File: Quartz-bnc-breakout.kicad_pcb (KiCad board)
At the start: 2 copper layers, 196.8 x 69.8 mm, 28 parts, among them J1 Conn_Coaxial, J10 Conn_Coaxial, J11 Conn_Coaxial, J12 Conn_Coaxial, J13 Conn_Coaxial, J14 Conn_Coaxial, J15 Conn_Coaxial, J16 Conn_Coaxial, J17 DC37_Pins_MountingHoles, J2 Conn_Coaxial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

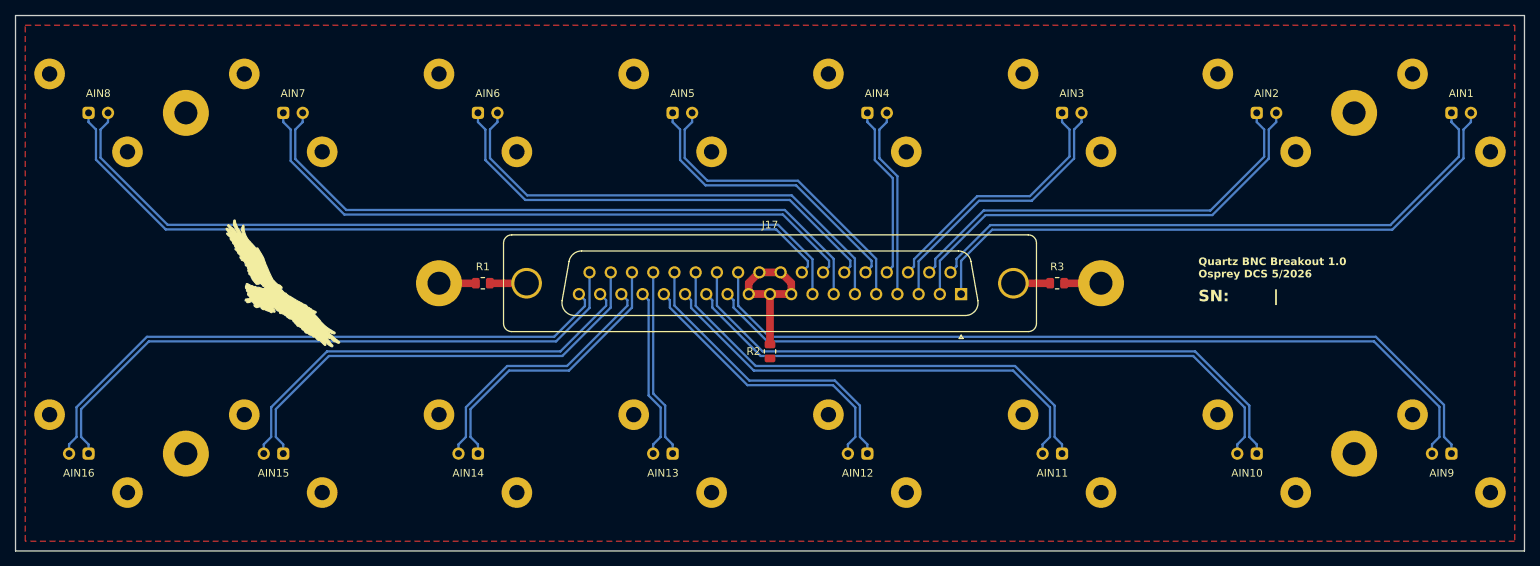
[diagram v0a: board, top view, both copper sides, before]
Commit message: Changed mounting hole footprints from 3mm to 3.4mm
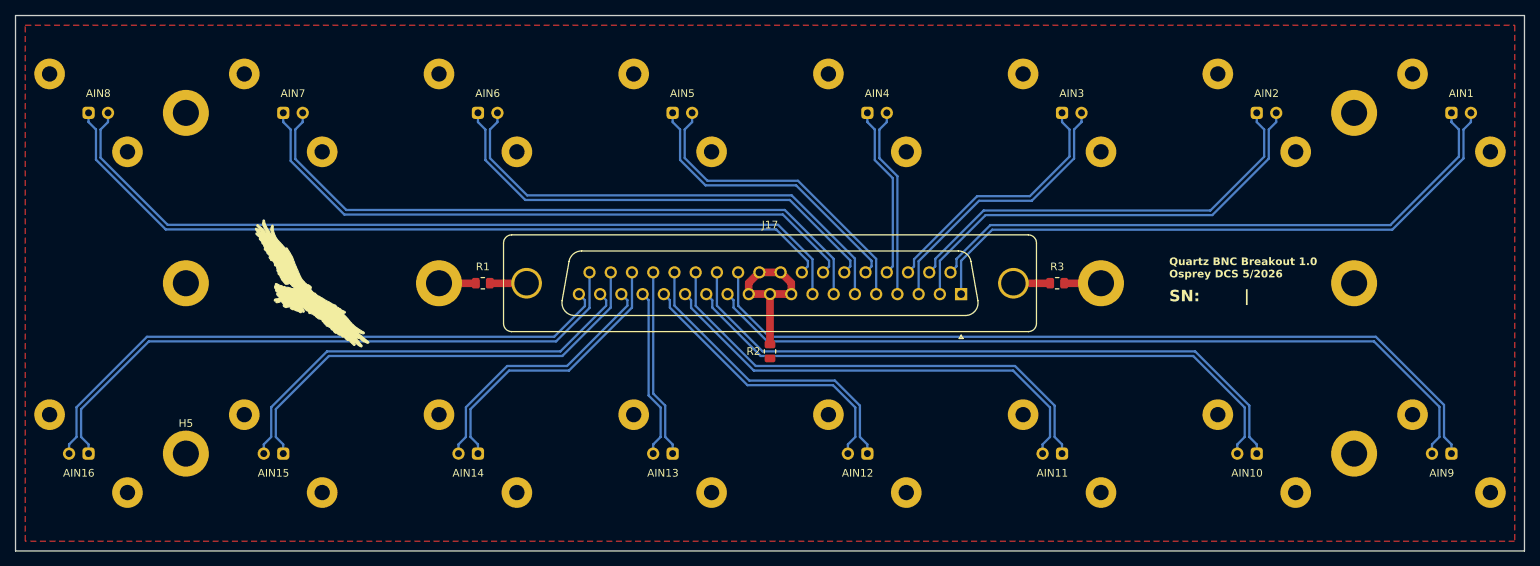
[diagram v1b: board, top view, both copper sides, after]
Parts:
- added H7: MountingHole_Pad, 0local:MountingHole_3.4mm_Pad, F.Cu at (63.5, 92.1)
- added H8: MountingHole_Pad, 0local:MountingHole_3.4mm_Pad, F.Cu at (215.9, 92.1)
- H1, H2, H3, H4, H5, H6: footprint 0local:MountingHole_3mm_Pad -> 0local:MountingHole_3.4mm_Pad
- moved Logo1 3.81 mm to (80.0, 92.7) (x2)

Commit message: Added more padding to D mounting holes
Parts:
- moved H8 79.4 mm to (139.7, 114.3)
- moved H7 79.4 mm to (139.7, 69.8)
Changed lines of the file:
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@@
 		(pad "SH1" thru_hole circle
 			(at -6.82 1.42 180)
-			(size 4 4)
+			(size 5 5)
 			(drill 3.2)
 			(layers "*.Cu" "*.Mask")
@@
 		(pad "SH2" thru_hole circle
 			(at 56.68 1.42 180)
-			(size 4 4)
+			(size 5 5)
 			(drill 3.2)
 			(layers "*.Cu" "*.Mask")
@@
 	(footprint "0local:MountingHole_3.4mm_Pad"
 		(layer "F.Cu")
-		(at 215.9 92.075)
+		(at 139.7 114.3)
 		(descr "Mounting Hole 3mm, generated by kicad-footprint-generator mountinghole.py")
 		(tags "mountinghole")
@@
 			(at 0 -3.95 0)
 			(layer "F.SilkS")
+			(hide yes)
 			(effects
 				(font
@@
 	(footprint "0local:MountingHole_3.4mm_Pad"
 		(layer "F.Cu")
-		(at 63.5 92.075)
+		(at 139.7 69.85)
 		(descr "Mounting Hole 3mm, generated by kicad-footprint-generator mountinghole.py")
 		(tags "mountinghole")
@@
 			(keep_text_aligned yes)
 		)
-		(gr_text "1.75 in"
+		(gr_text "44.45 mm"
 			(at 33.14 92.075 90)
 			(layer "User.1")
@@
 			(keep_text_aligned yes)
 		)
-		(gr_text "7.75 in"
+		(gr_text "196.85 mm"
 			(at 139.7 40.76 0)
 			(layer "User.1")
@@
 			(keep_text_aligned yes)
 		)
-		(gr_text "2.75 in"
+		(gr_text "69.85 mm"
 			(at 250.31 92.075 90)
 			(layer "User.1")

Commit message: Updated correct D connector
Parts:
- moved J17 24.9 mm to (139.7, 93.5)

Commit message: minor changes
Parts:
- removed the Logo1 at (80.0, 92.7)
- moved Logo1 15.9 mm to (64.1, 92.1)
- moved H4 7.62 mm to (190.5, 92.1)
- moved H3 7.62 mm to (88.9, 92.1)
- moved H1 3.18 mm to (63.5, 73.0)
- moved H2 3.18 mm to (215.9, 73.0)
- moved H7 3.18 mm to (139.7, 73.0)
- moved J1 3.18 mm to (228.6, 73.0)
- moved J2 3.18 mm to (203.2, 73.0)
- moved J3 3.18 mm to (177.8, 73.0)
- moved J4 3.18 mm to (152.4, 73.0)
- moved J5 3.18 mm to (127.0, 73.0)
- moved J6 3.18 mm to (101.6, 73.0)
- moved J7 3.18 mm to (76.2, 73.0)
- moved J8 3.18 mm to (50.8, 73.0)
- moved H5 3.17 mm to (63.5, 111.1)
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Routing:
- net Earth: track 9.61 -> 0.00 mm
- net /AIN14-: track 34.9 -> 31.7 mm
- net /AIN15-: track 57.5 -> 54.3 mm
- net /AIN16-: track 80.2 -> 77.0 mm
- net /AIN4-: track 25.0 -> 21.8 mm
- net /AIN4+: track 22.5 -> 19.3 mm
- net /AIN2+: track 56.8 -> 53.6 mm
- net /AIN1-: track 81.8 -> 78.6 mm
- net /AIN1+: track 79.4 -> 76.2 mm
- net /AIN3+: track 34.1 -> 31.0 mm
- net /AIN13+: track 24.7 -> 21.5 mm
- net /AIN16+: track 82.7 -> 79.5 mm
- net /AIN15+: track 60.0 -> 56.8 mm
- net /AIN14+: track 37.4 -> 34.2 mm
- net /AIN13-: track 22.2 -> 19.0 mm
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- added copper zone on B.Cu, net Earth
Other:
- board size 196.8 x 69.8 mm -> 196.8 x 63.5 mm
- board text added: "Quartz BNC Breakout 1.0 Osprey DCS 2026"
- board text removed: "Quartz BNC Breakout 1.0 Osprey DCS 5/2026"
